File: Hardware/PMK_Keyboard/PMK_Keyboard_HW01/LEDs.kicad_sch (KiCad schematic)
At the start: 40 parts

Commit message: Started routing
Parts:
- removed D633, D634, D635, D636, D637, D638, D639, D640: YF923_2020_WS2812_LED, Component_lib:YF923_2020_WS2812_LED_DUALSIDE, symbol Component lib:YF923_2020_WS2812_LED
- renumbered D601 to D401, D602 to D402, D603 to D403, D604 to D404, D605 to D405, D606 to D406, D607 to D407, D608 to D408, D609 to D409, D610 to D410, D611 to D411, D612 to D412, D613 to D413, D614 to D414, D615 to D415, D616 to D416, D617 to D417, D618 to D418, D619 to D419, D620 to D420, D621 to D421, D622 to D422, D623 to D423, D624 to D424, D625 to D425, D626 to D426, D627 to D427, D628 to D428, D629 to D429, D630 to D430, D631 to D431, D632 to D432
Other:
- note added: "400- LEDs"
- note removed: "600- LEDs"

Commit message: working on routing
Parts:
- removed D430, D431, D432: YF923_2020_WS2812_LED, Component_lib:YF923_2020_WS2812_LED_DUALSIDE, symbol Component lib:YF923_2020_WS2812_LED

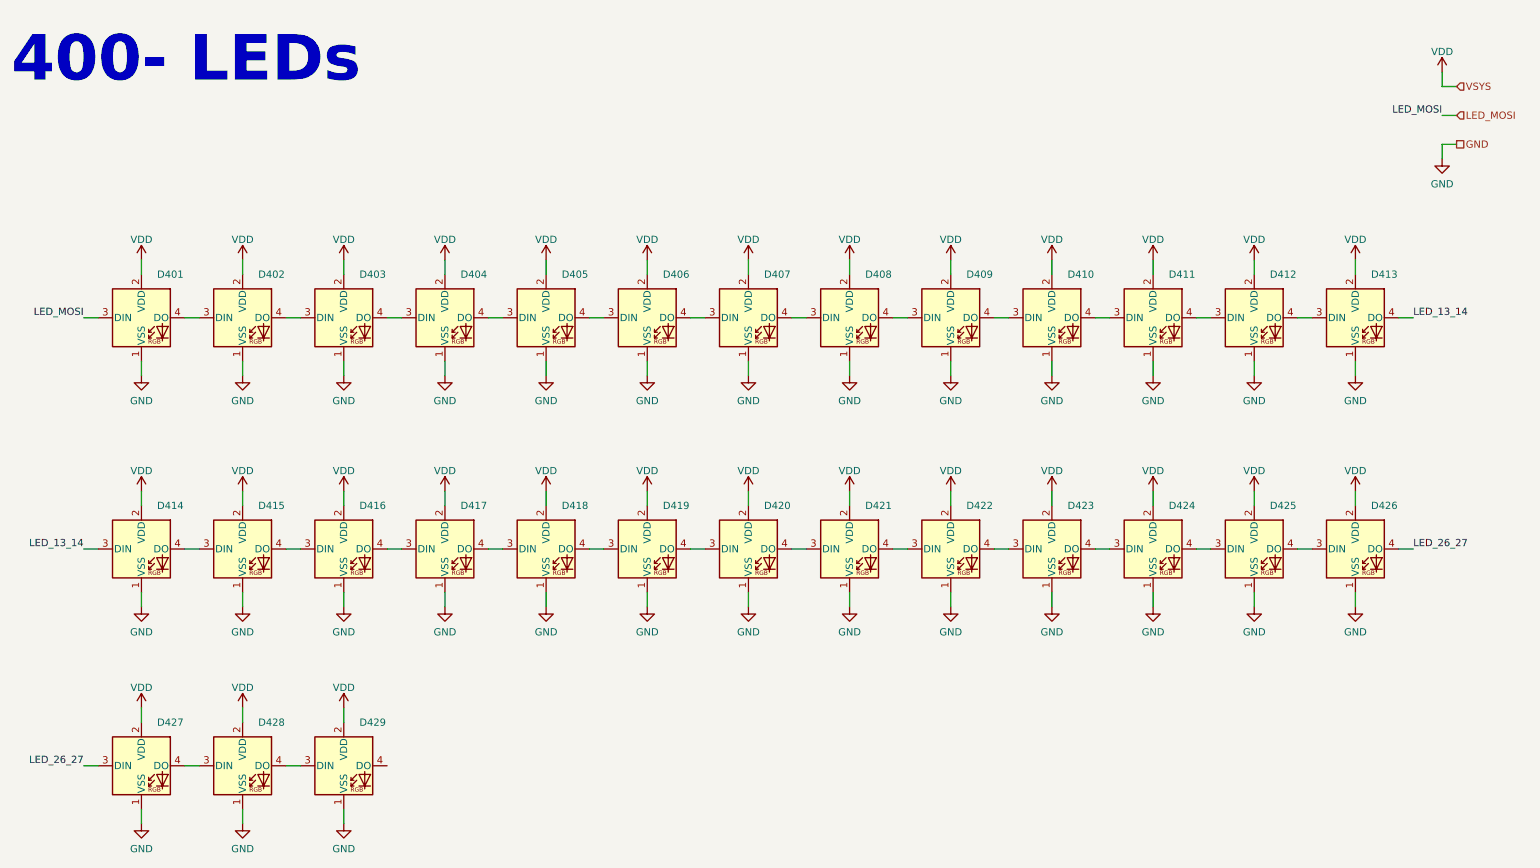
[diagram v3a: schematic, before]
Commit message: added mounting holes + fix in ref des
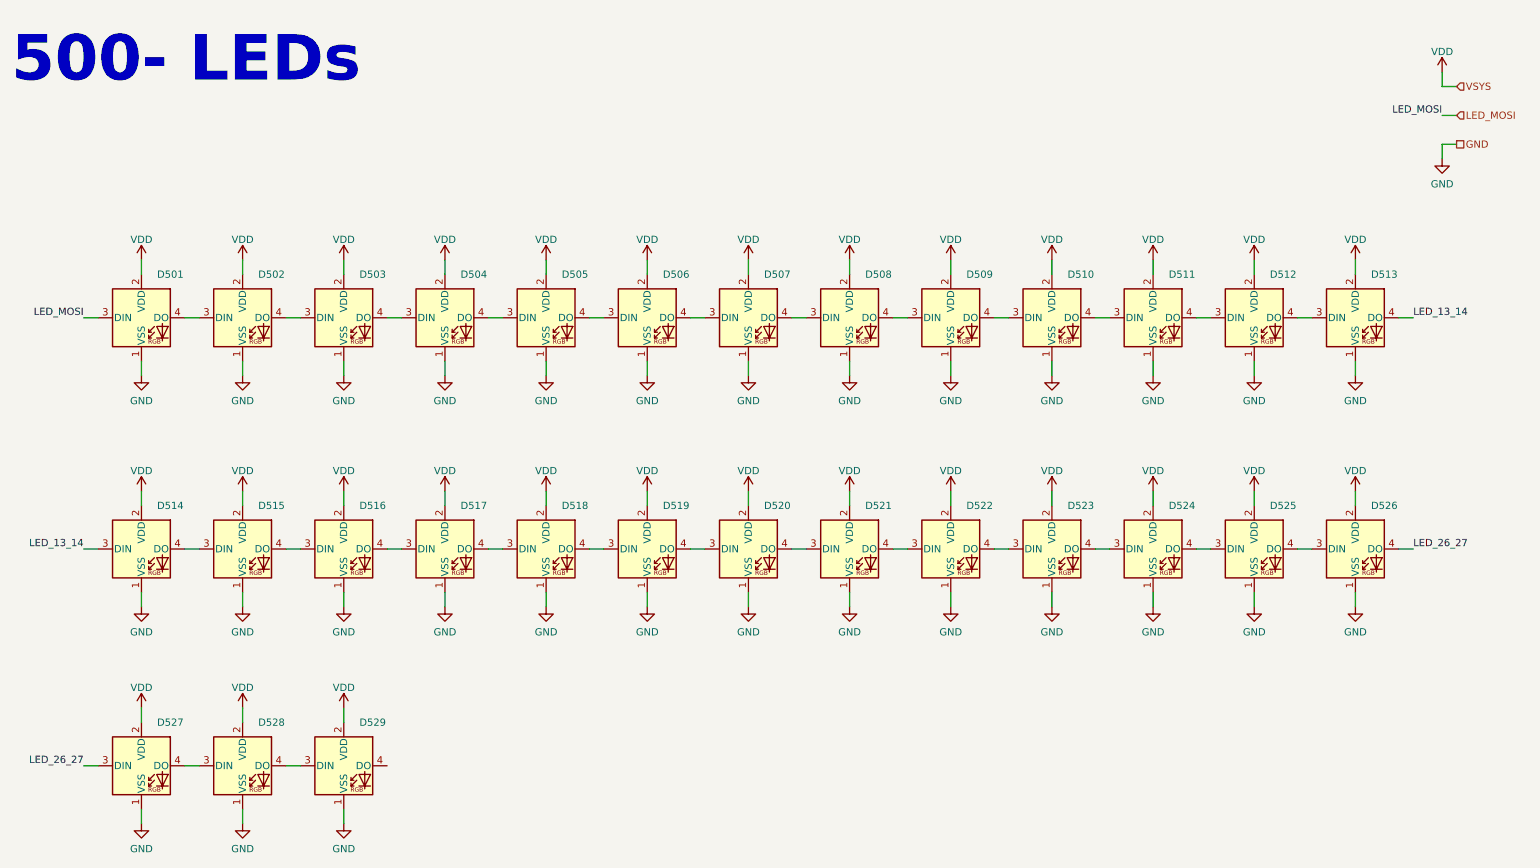
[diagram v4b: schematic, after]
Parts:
- renumbered D401 to D501, D402 to D502, D403 to D503, D404 to D504, D405 to D505, D406 to D506, D407 to D507, D408 to D508, D409 to D509, D410 to D510, D411 to D511, D412 to D512, D413 to D513, D414 to D514, D415 to D515, D416 to D516, D417 to D517, D418 to D518, D419 to D519, D420 to D520, D421 to D521, D422 to D522, D423 to D523, D424 to D524, D425 to D525, D426 to D526, D427 to D527, D428 to D528, D429 to D529
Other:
- note added: "500- LEDs"
- note removed: "400- LEDs"
